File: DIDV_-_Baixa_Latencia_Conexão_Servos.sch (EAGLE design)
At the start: 205 parts

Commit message: Revisão 7:
-  Alterações necessárias para adequação às necessidades dos exemplos de controle que temos.
-  Revisão da forma de filtragem de sinais digitais
-  Algumas nomenclaturas ainda estão erradas, deverão ser corrigidas com o andamento da implementação.
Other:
- note added: "07"
- note removed: "06"
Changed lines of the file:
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@@
 <text x="203.2" y="29.464" size="1.778" layer="150" font="vector">Dispositivo de Interface para</text>
 <text x="210.82" y="26.162" size="1.778" layer="150" font="vector">Deficientes Visuais</text>
-<text x="250.698" y="10.16" size="2.54" layer="150" font="vector">06</text>
+<text x="250.698" y="10.16" size="2.54" layer="150" font="vector">07</text>
 <text x="7.62" y="127" size="1.778" layer="150" font="vector">Alimentacao</text>
 <text x="68.58" y="109.22" size="1.778" layer="150" font="vector" rot="R90">Conector dos acionamentos</text>
@@
 <text x="203.2" y="29.464" size="1.778" layer="150" font="vector">Dispositivo de Interface para</text>
 <text x="210.82" y="26.162" size="1.778" layer="150" font="vector">Deficientes Visuais</text>
-<text x="250.698" y="10.16" size="2.54" layer="150" font="vector">06</text>
+<text x="250.698" y="10.16" size="2.54" layer="150" font="vector">07</text>
 </plain>
 <instances>
@@
 <text x="203.2" y="29.464" size="1.778" layer="150" font="vector">Dispositivo de Interface para</text>
 <text x="210.82" y="26.162" size="1.778" layer="150" font="vector">Deficientes Visuais</text>
-<text x="250.698" y="10.16" size="2.54" layer="150" font="vector">06</text>
+<text x="250.698" y="10.16" size="2.54" layer="150" font="vector">07</text>
 </plain>
 <instances>

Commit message: Revisão 8:
-  Add Circuito Buck
-  Alterações funcionais
-   Inserção dos primeiros boards
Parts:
- removed C301, C302, C303, C304, C305, C306, C307, C308, C309, C310, C311, C312, C313, C314, C315, C316, C317, C318, C319, C320, C321, C322, C323, C324, C325, C326, C327, C328, C329, C330, C331, C332: 100pf/50V, rcl:C-USC0603
- removed JP103, JP104: (no value), jumper:JP8Q
- removed JP141, JP142, JP143, JP144, JP145, JP146, JP147, JP148, JP149, JP150, JP151, JP152, JP153, JP154, JP155, JP156, JP157, JP158, JP159, JP160, JP161, JP162, JP163, JP164, JP165, JP166, JP167, JP168, JP169, JP170, JP171, JP172: (no value), jumper:JP2E
- removed LOGO301: OSHW-LOGOM, SparkFun-Aesthetics:OSHW-LOGOM
- removed R301, R302, R303, R304, R305, R306, R307, R308, R309, R310, R311, R312, R313, R314, R315, R316, R317, R318, R319, R320, R321, R322, R323, R324, R325, R326, R327, R328, R329, R330, R331, R332: 22, rcl:R-US_R0603
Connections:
- removed net M32: JP103.2, R301.1
- removed net M32_: C301.1, JP141.3, R301.2
- removed net M33: JP103.4, R302.1
- removed net M33_: C302.1, JP142.3, R302.2
- removed net M34: JP103.6, R303.1
- removed net M34_: C303.1, JP143.3, R303.2
- removed net M35: JP103.8, R304.1
- removed net M35_: C304.1, JP144.3, R304.2
- removed net M36: JP103.10, R305.1
- removed net M36_: C305.1, JP145.3, R305.2
- removed net M37: JP103.12, R306.1
- removed net M37_: C306.1, JP146.3, R306.2
- removed net M38: JP103.14, R307.1
- removed net M38_: C307.1, JP147.3, R307.2
- removed net M39: JP103.16, R308.1
- removed net M39_: C308.1, JP148.3, R308.2
- removed net M40: JP103.15, R309.1
- removed net M40_: C309.1, JP149.3, R309.2
- removed net M41: JP103.13, R310.1
- removed net M41_: C310.1, JP150.3, R310.2
- removed net M42: JP103.11, R311.1
- removed net M42_: C311.1, JP151.3, R311.2
- removed net M43: JP103.9, R312.1
- removed net M43_: C312.1, JP152.3, R312.2
- removed net M44: JP103.7, R313.1
- removed net M44_: C313.1, JP153.3, R313.2
- removed net M45: JP103.5, R314.1
- removed net M45_: C314.1, JP154.3, R314.2
- removed net M46: JP103.3, R315.1
- removed net M46_: C315.1, JP155.3, R315.2
- removed net M47: JP103.1, R316.1
- removed net M47_: C316.1, JP156.3, R316.2
- removed net M48: JP104.2, R317.1
- removed net M48_: C317.1, JP157.3, R317.2
- removed net M49: JP104.4, R318.1
- removed net M49_: C318.1, JP159.3, R318.2
- removed net M50: JP104.6, R319.1
- removed net M50_: C319.1, JP161.3, R319.2
- removed net M51: JP104.8, R320.1
- removed net M51_: C320.1, JP163.3, R320.2
- removed net M52: JP104.10, R321.1
- removed net M52_: C321.1, JP165.3, R321.2
- removed net M53: JP104.12, R322.1
- removed net M53_: C322.1, JP167.3, R322.2
- removed net M54: JP104.14, R323.1
- removed net M54_: C323.1, JP168.3, R323.2
- removed net M55: JP104.16, R324.1
- removed net M55_: C324.1, JP169.3, R324.2
- removed net M56: JP104.15, R325.1
- removed net M56_: C325.1, JP170.3, R325.2
- removed net M57: JP104.13, R326.1
- removed net M57_: C326.1, JP171.3, R326.2
- removed net M58: JP104.11, R327.1
- removed net M58_: C327.1, JP172.3, R327.2
- removed net M59: JP104.9, R328.1
- removed net M59_: C328.1, JP158.3, R328.2
- removed net M60: JP104.7, R329.1
- removed net M60_: C329.1, JP160.3, R329.2
- removed net M61: JP104.5, R330.1
- removed net M61_: C330.1, JP162.3, R330.2
- removed net M62: JP104.3, R331.1
- removed net M62_: C331.1, JP164.3, R331.2
- removed net M63: JP104.1, R332.1
- removed net M63_: C332.1, JP166.3, R332.2
- removed net VCC: C101.1, C102.1, JP105.1, JP105.2, JP106.1, JP106.2, JP109.2, JP110.2, JP111.2, JP112.2, JP113.2, JP114.2, JP115.2, JP116.2, JP117.2, JP118.2, JP119.2, JP120.2, JP121.2, JP122.2, JP123.2, JP124.2, JP125.2, JP126.2, JP127.2, JP128.2, JP129.2, JP130.2, JP131.2, JP132.2, JP133.2, JP134.2, JP135.2, JP136.2, JP137.2, JP138.2, JP139.2, JP140.2, JP141.2, JP142.2, JP143.2, JP144.2, JP145.2, JP146.2, JP147.2, JP148.2, JP149.2, JP150.2, JP151.2, JP152.2, JP153.2, JP154.2, JP155.2, JP156.2, JP157.2, JP158.2, JP159.2, JP160.2, JP161.2, JP162.2, JP163.2, JP164.2, JP165.2, JP166.2, JP167.2, JP168.2, JP169.2, JP170.2, JP171.2, JP172.2
- new net +6V: C101.1, C102.1, JP105.1, JP105.2, JP106.1, JP106.2, JP109.2, JP110.2, JP111.2, JP112.2, JP113.2, JP114.2, JP115.2, JP116.2, JP117.2, JP118.2, JP119.2, JP120.2, JP121.2, JP122.2, JP123.2, JP124.2, JP125.2, JP126.2, JP127.2, JP128.2, JP129.2, JP130.2, JP131.2, JP132.2, JP133.2, JP134.2, JP135.2, JP136.2, JP137.2, JP138.2, JP139.2, JP140.2
- net AGND: no longer C301.2, C302.2, C303.2, C304.2, C305.2, C306.2, C307.2, C308.2, C309.2, C310.2, C311.2, C312.2, C313.2, C314.2, C315.2, C316.2, C317.2, C318.2, C319.2, C320.2, C321.2, C322.2, C323.2, C324.2, C325.2, C326.2, C327.2, C328.2, C329.2, C330.2, C331.2, C332.2, JP141.1, JP142.1, JP143.1, JP144.1, JP145.1, JP146.1, JP147.1, JP148.1, JP149.1, JP150.1, JP151.1, JP152.1, JP153.1, JP154.1, JP155.1, JP156.1, JP157.1, JP158.1, JP159.1, JP160.1, JP161.1, JP162.1, JP163.1, JP164.1, JP165.1, JP166.1, JP167.1, JP168.1, JP169.1, JP170.1, JP171.1, JP172.1
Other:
- note added: "08"
- note removed: "07"

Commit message: Revisão 9
- Corrigidos algumas falhas de ligação
- Implementação com VPRG dos TLCs via Hardware
- Inserção do cálculo do Riref

Obs. Se somente a criação de boards, não será incrementado. No caso, se criado um board novo board vou subir para 9.1 e assim por diante.
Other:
- note added: "09"
- note removed: "08"
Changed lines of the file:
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@@
 <text x="203.2" y="29.464" size="1.778" layer="150" font="vector">Dispositivo de Interface para</text>
 <text x="210.82" y="26.162" size="1.778" layer="150" font="vector">Deficientes Visuais</text>
-<text x="250.698" y="10.16" size="2.54" layer="150" font="vector">08</text>
+<text x="250.698" y="10.16" size="2.54" layer="150" font="vector">09</text>
 <text x="7.62" y="127" size="1.778" layer="150" font="vector">Alimentacao</text>
 <text x="68.58" y="109.22" size="1.778" layer="150" font="vector" rot="R90">Conector dos acionamentos</text>
@@
 <text x="203.2" y="29.464" size="1.778" layer="150" font="vector">Dispositivo de Interface para</text>
 <text x="210.82" y="26.162" size="1.778" layer="150" font="vector">Deficientes Visuais</text>
-<text x="250.698" y="10.16" size="2.54" layer="150" font="vector">08</text>
+<text x="250.698" y="10.16" size="2.54" layer="150" font="vector">09</text>
 </plain>
 <instances>

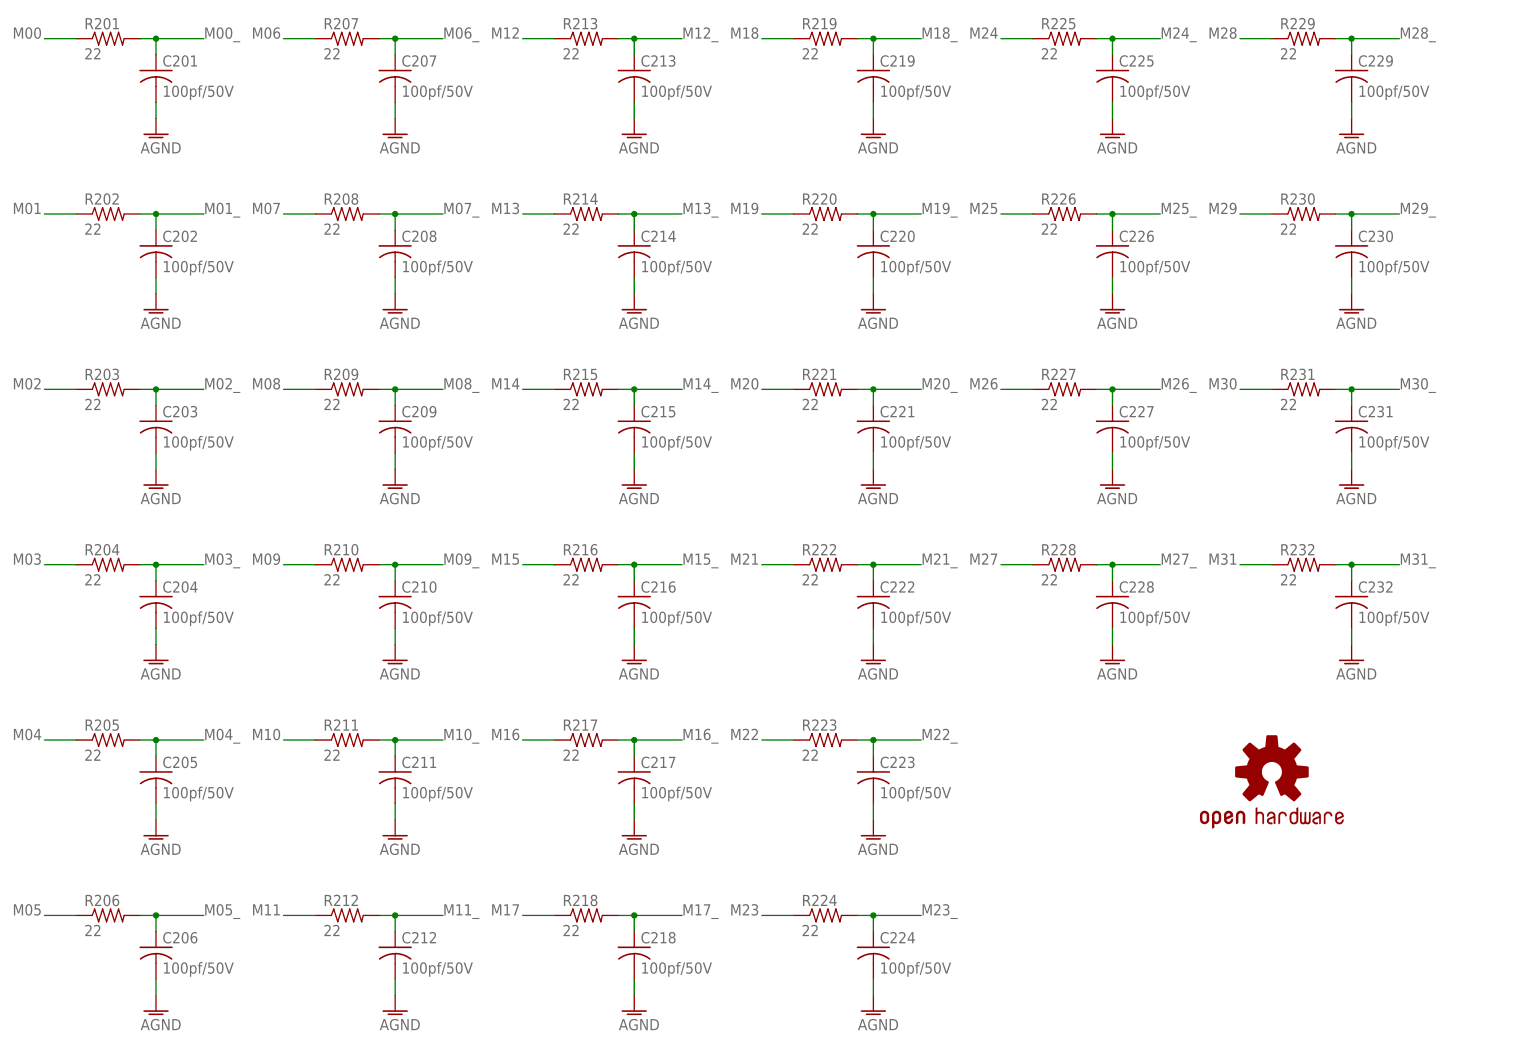
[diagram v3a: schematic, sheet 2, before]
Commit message: Revisão 10
Revisão representa o estado final do projeto, alterações agora somente referentes a valores de componentes e adaptações se e somente se não existir a possibilidade de manobras via software.

Placas nas dimensões e condições as quais foram submetidas a cotação para confecção em local especializado.
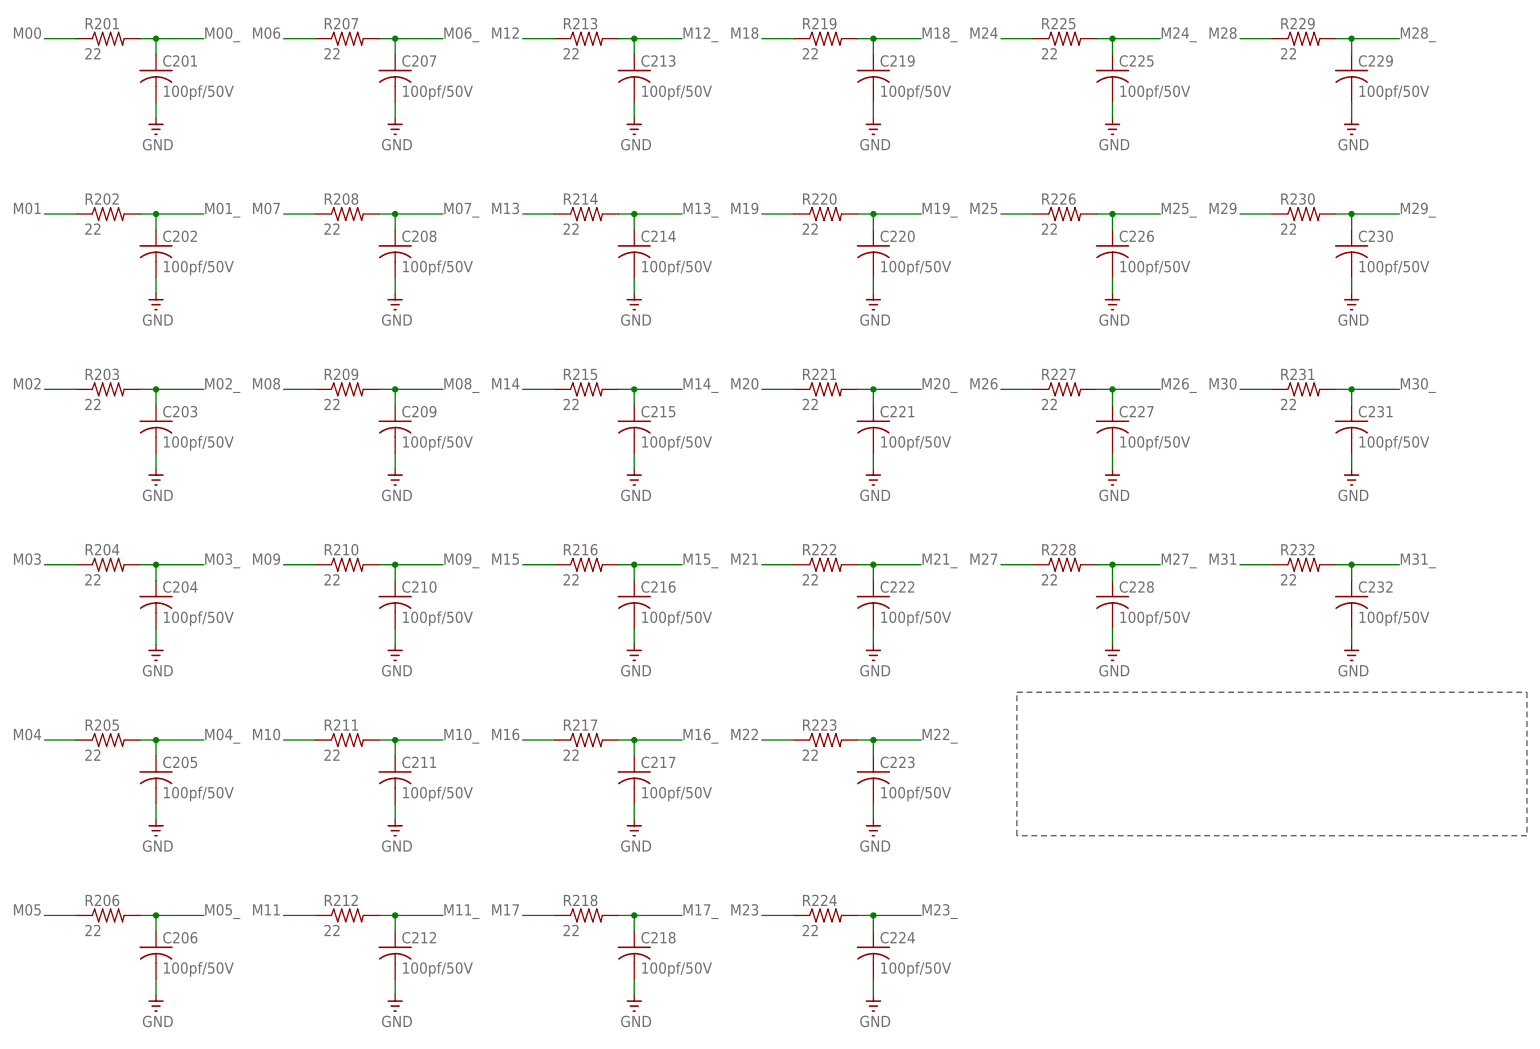
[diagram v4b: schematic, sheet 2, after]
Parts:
- removed C102: 100nf/50V, rcl:C-EUC0805K
- removed JP139, JP140: (no value), jumper:JP2E
- removed LOGO201: OSHW-LOGOM, SparkFun-Aesthetics:OSHW-LOGOM
- added JP103, JP104: (no value), jumper:JP1E
- C101: value 100nf/50V -> 470uf/50V; device rcl:C-EUC0805K -> rcl:CPOL-US140CLH-1010
- JP107, JP108: device jumper:JP1E -> jumper:JP2E
- LOGO101: value OSHW-LOGOM -> OSHW-LOGOL; device SparkFun-Aesthetics:OSHW-LOGOM -> OpenHW_BOT:OSHW-LOGOL
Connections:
- removed net AGND: C101.2, C102.2, C201.2, C202.2, C203.2, C204.2, C205.2, C206.2, C207.2, C208.2, C209.2, C210.2, C211.2, C212.2, C213.2, C214.2, C215.2, C216.2, C217.2, C218.2, C219.2, C220.2, C221.2, C222.2, C223.2, C224.2, C225.2, C226.2, C227.2, C228.2, C229.2, C230.2, C231.2, C232.2, JP107.1, JP107.2, JP108.1, JP108.2, JP109.1, JP110.1, JP111.1, JP112.1, JP113.1, JP114.1, JP115.1, JP116.1, JP117.1, JP118.1, JP119.1, JP120.1, JP121.1, JP122.1, JP123.1, JP124.1, JP125.1, JP126.1, JP127.1, JP128.1, JP129.1, JP130.1, JP131.1, JP132.1, JP133.1, JP134.1, JP135.1, JP136.1, JP137.1, JP138.1, JP139.1, JP140.1
- new net GND: C101.-, C201.2, C202.2, C203.2, C204.2, C205.2, C206.2, C207.2, C208.2, C209.2, C210.2, C211.2, C212.2, C213.2, C214.2, C215.2, C216.2, C217.2, C218.2, C219.2, C220.2, C221.2, C222.2, C223.2, C224.2, C225.2, C226.2, C227.2, C228.2, C229.2, C230.2, C231.2, C232.2, JP105.1, JP105.2, JP106.1, JP106.2, JP107.1, JP108.1, JP109.1, JP110.1, JP111.1, JP112.1, JP113.1, JP114.1, JP115.1, JP116.1, JP117.1, JP118.1, JP119.1, JP120.1, JP121.1, JP122.1, JP123.1, JP124.1, JP125.1, JP126.1, JP127.1, JP128.1, JP129.1, JP130.1, JP131.1, JP132.1, JP133.1, JP134.1, JP135.1, JP136.1, JP137.1, JP138.1
- net +6V: now also C101.+, JP103.1, JP103.2, JP104.1, JP104.2, JP107.2, JP108.2; no longer C101.1, C102.1, JP105.1, JP105.2, JP106.1, JP106.2, JP139.2, JP140.2
- net M00: now also JP102.1; no longer JP101.2
- net M00_: now also JP107.3; no longer JP109.3
- net M01: now also JP102.2; no longer JP101.4
- net M01_: now also JP108.3; no longer JP110.3
- net M02: now also JP102.3; no longer JP101.6
- net M02_: now also JP109.3; no longer JP111.3
- net M03: now also JP102.4; no longer JP101.8
- net M03_: now also JP110.3; no longer JP112.3
- net M04: now also JP102.5; no longer JP101.10
- net M04_: now also JP111.3; no longer JP113.3
- net M05: now also JP102.6; no longer JP101.12
- net M05_: now also JP112.3; no longer JP114.3
- net M06: now also JP102.7; no longer JP101.14
- net M06_: now also JP113.3; no longer JP115.3
- net M07: now also JP102.8; no longer JP101.16
- net M07_: now also JP114.3; no longer JP116.3
- net M08: now also JP102.9; no longer JP101.15
- net M08_: now also JP115.3; no longer JP117.3
- net M09: now also JP102.10; no longer JP101.13
- net M09_: now also JP116.3; no longer JP118.3
- net M10: now also JP102.11; no longer JP101.11
- net M10_: now also JP117.3; no longer JP119.3
- net M11: now also JP102.12; no longer JP101.9
- net M11_: now also JP118.3; no longer JP120.3
- net M12: now also JP102.13; no longer JP101.7
- net M12_: now also JP119.3; no longer JP121.3
- net M13: now also JP102.14; no longer JP101.5
- net M13_: now also JP120.3; no longer JP122.3
- net M14: now also JP102.15; no longer JP101.3
- net M14_: now also JP121.3; no longer JP123.3
- net M15: now also JP102.16; no longer JP101.1
- net M15_: now also JP122.3; no longer JP124.3
- net M16: now also JP101.1; no longer JP102.2
- net M16_: now also JP123.3; no longer JP125.3
- net M17: now also JP101.2; no longer JP102.4
- net M17_: now also JP124.3; no longer JP126.3
- net M18: now also JP101.3; no longer JP102.6
- net M18_: now also JP125.3; no longer JP127.3
- net M19: now also JP101.4; no longer JP102.8
- net M19_: now also JP126.3; no longer JP128.3
- net M20: now also JP101.5; no longer JP102.10
- net M20_: now also JP127.3; no longer JP129.3
- net M21: now also JP101.6; no longer JP102.12
- net M21_: now also JP128.3; no longer JP130.3
- net M22: now also JP101.7; no longer JP102.14
- net M22_: now also JP129.3; no longer JP131.3
- net M23: now also JP101.8; no longer JP102.16
- net M23_: now also JP130.3; no longer JP132.3
- net M24: now also JP101.9; no longer JP102.15
- net M24_: now also JP131.3; no longer JP133.3
- net M25: now also JP101.10; no longer JP102.13
- net M25_: now also JP132.3; no longer JP134.3
- net M26: now also JP101.11; no longer JP102.11
- net M26_: now also JP133.3; no longer JP135.3
- net M27: now also JP101.12; no longer JP102.9
- net M27_: now also JP134.3; no longer JP136.3
- net M28: now also JP101.13; no longer JP102.7
- net M28_: now also JP135.3; no longer JP137.3
- net M29: now also JP101.14; no longer JP102.5
- net M29_: now also JP136.3; no longer JP138.3
- net M30: now also JP101.15; no longer JP102.3
- net M30_: now also JP137.3; no longer JP139.3
- net M31: now also JP101.16; no longer JP102.1
- net M31_: now also JP138.3; no longer JP140.3
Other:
- note added: "10"
- note added: "Os filtros devem ser implementados"
- note added: "Para um filtro passa baixa com 100Hz"
- note added: "Se e somente se necessário"
- note added: "de FC, os valores sao: R=1k5 e C=1uF"
- note removed: "09"
- moved on the sheet: JP101, JP102, JP105, JP106, JP109, JP110, JP111, JP112, JP113, JP114, JP115, JP116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
